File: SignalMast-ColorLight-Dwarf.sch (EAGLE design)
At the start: 4 parts

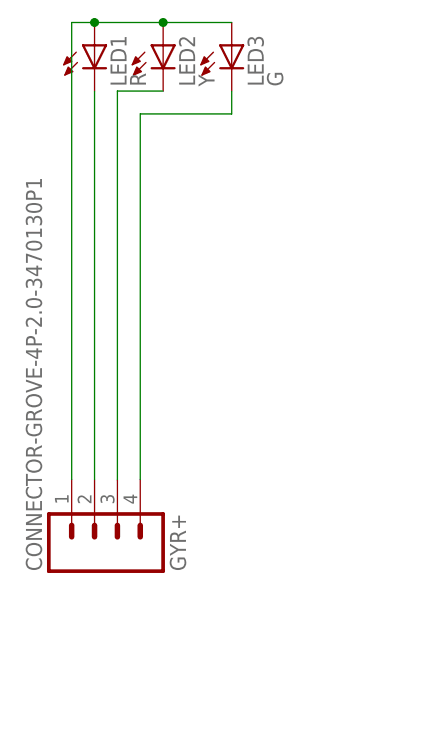
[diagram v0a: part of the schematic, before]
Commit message: normalized values
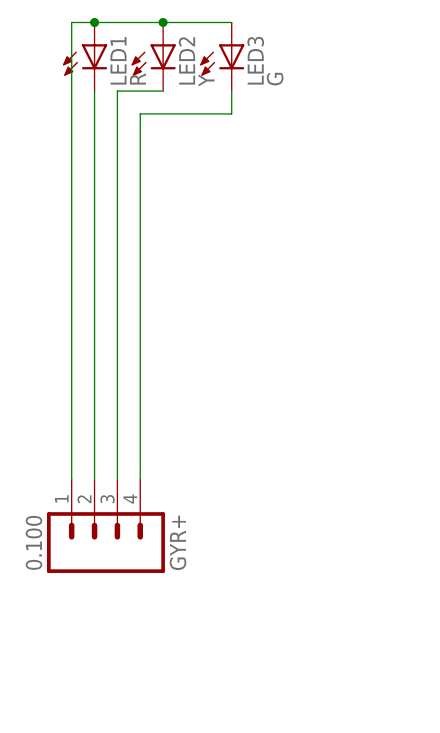
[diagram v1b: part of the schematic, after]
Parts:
- GYR+: value CONNECTOR-GROVE-4P-2.0-3470130P1 -> 0.100
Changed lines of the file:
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@@
 <parts>
 <part name="FRAME2" library="SPCoast" deviceset="DOC-FRAME-LETTER" device=""/>
-<part name="GYR+" library="SPCoast" deviceset="CONNECTOR-M04" device="LOCK" value="CONNECTOR-GROVE-4P-2.0-3470130P1"/>
+<part name="GYR+" library="SPCoast" deviceset="CONNECTOR-M04" device="LOCK" value="0.100"/>
 <part name="LED1" library="SPCoast" deviceset="LED*" device="0603-LED" value="R">
 <attribute name="OPL" value="19-217-R6C-AL1M2VY-3T"/>
